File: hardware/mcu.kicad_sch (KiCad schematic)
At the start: 11 parts, among them J12 PICO UTIL, U1 Pico 2

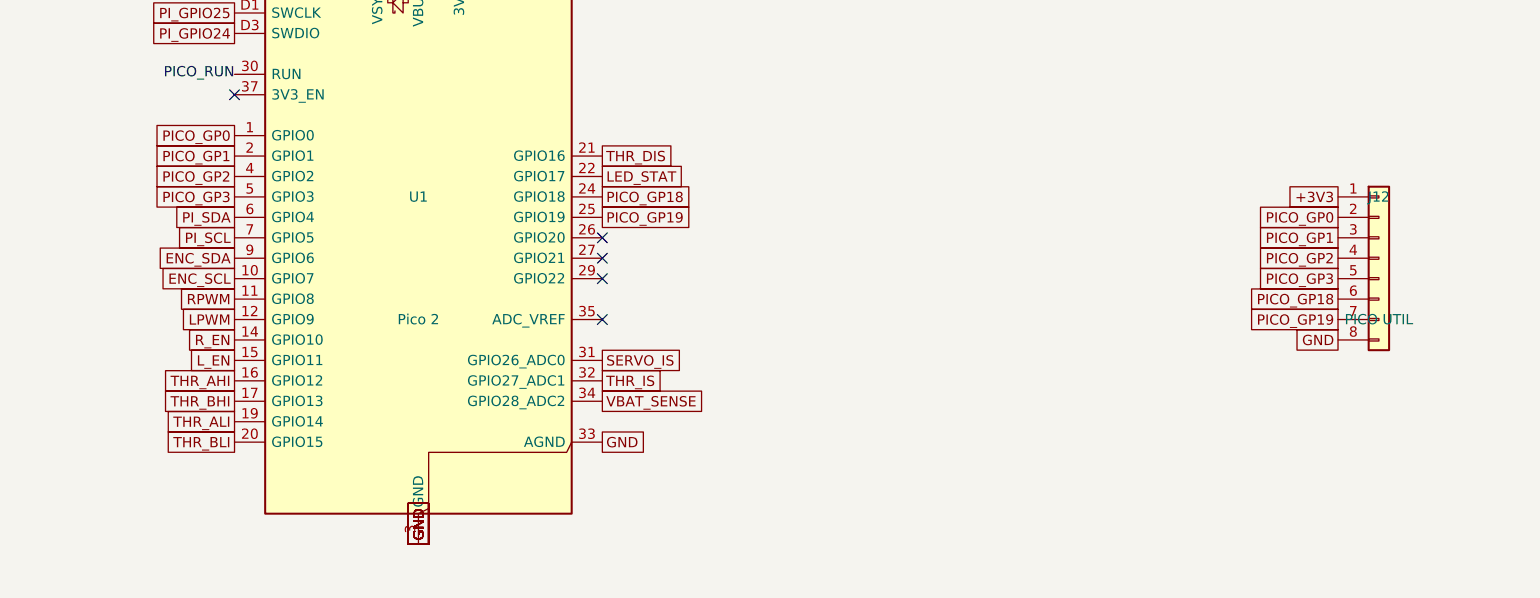
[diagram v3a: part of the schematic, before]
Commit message: cost pass 10 (schematic): remove on-board H-bridge, add J13 external-driver header (IBT-2 pinout); ERC 0, gate PASS
Co-Authored-By: Claude Fable 5 <noreply@anthropic.com>
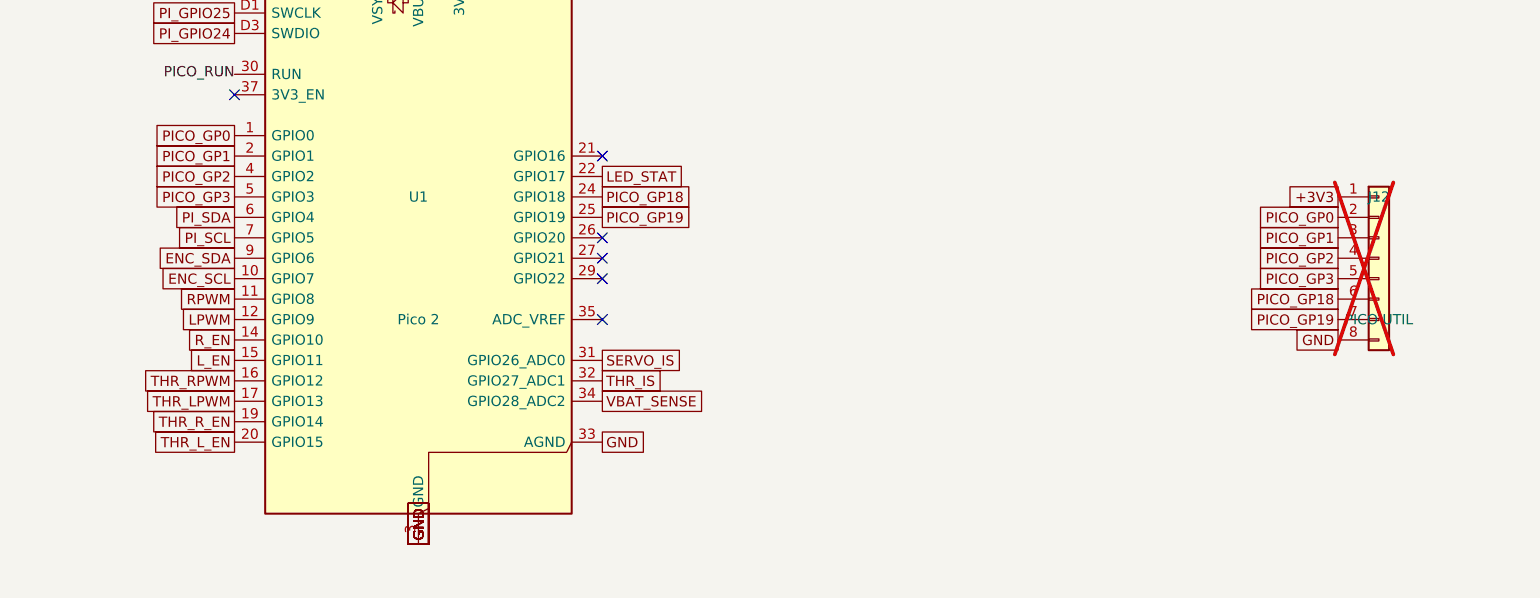
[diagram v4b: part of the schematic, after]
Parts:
- J12: now not fitted
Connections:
- net THR_AHI renamed THR_RPWM
- net THR_ALI renamed THR_R_EN
- net THR_BHI renamed THR_LPWM
- net THR_BLI renamed THR_L_EN
- net THR_DIS: no longer names the net of U1.21 (GPIO16)
- no-connect marks 6 -> 7
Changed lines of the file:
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@@
   )
   (symbol (lib_id "Connector_Generic:Conn_01x08") (at 199.39 110.49 0) (unit 1)
-    (exclude_from_sim no) (in_bom yes) (on_board yes) (dnp no)
+    (exclude_from_sim no) (in_bom yes) (on_board yes) (dnp yes)
     (property "Reference" "J12" (at 199.39 102.87 0)
       (effects (font (size 1.27 1.27))))
@@
       (effects (font (size 1.27 1.27)) (hide yes)))
   )
-  (global_label "THR_AHI" (shape passive) (at 57.15 125.73 180.0) (fields_autoplaced yes)
+  (global_label "THR_RPWM" (shape passive) (at 57.15 125.73 180.0) (fields_autoplaced yes)
     (effects (font (size 1.27 1.27)) (justify right))
     (property "Intersheetrefs" "${INTERSHEET_REFS}" (at 57.15 125.73 0)
       (effects (font (size 1.27 1.27)) (hide yes)))
   )
-  (global_label "THR_BHI" (shape passive) (at 57.15 128.27 180.0) (fields_autoplaced yes)
+  (global_label "THR_LPWM" (shape passive) (at 57.15 128.27 180.0) (fields_autoplaced yes)
     (effects (font (size 1.27 1.27)) (justify right))
     (property "Intersheetrefs" "${INTERSHEET_REFS}" (at 57.15 128.27 0)
@@
       (effects (font (size 1.27 1.27)) (hide yes)))
   )
-  (global_label "THR_ALI" (shape passive) (at 57.15 130.81 180.0) (fields_autoplaced yes)
+  (global_label "THR_R_EN" (shape passive) (at 57.15 130.81 180.0) (fields_autoplaced yes)
     (effects (font (size 1.27 1.27)) (justify right))
     (property "Intersheetrefs" "${INTERSHEET_REFS}" (at 57.15 130.81 0)
       (effects (font (size 1.27 1.27)) (hide yes)))
   )
-  (global_label "THR_BLI" (shape passive) (at 57.15 133.35 180.0) (fields_autoplaced yes)
+  (global_label "THR_L_EN" (shape passive) (at 57.15 133.35 180.0) (fields_autoplaced yes)
     (effects (font (size 1.27 1.27)) (justify right))
     (property "Intersheetrefs" "${INTERSHEET_REFS}" (at 57.15 133.35 0)
       (effects (font (size 1.27 1.27)) (hide yes)))
   )
-  (global_label "THR_DIS" (shape passive) (at 102.87 97.79 0.0) (fields_autoplaced yes)
-    (effects (font (size 1.27 1.27)) (justify left))
-    (property "Intersheetrefs" "${INTERSHEET_REFS}" (at 102.87 97.79 0)
-      (effects (font (size 1.27 1.27)) (hide yes)))
-  )
   (global_label "LED_STAT" (shape passive) (at 102.87 100.33 0.0) (fields_autoplaced yes)
     (effects (font (size 1.27 1.27)) (justify left))
@@
       (effects (font (size 1.27 1.27)) (hide yes)))
   )
+  (no_connect (at 102.87 97.79))
   (no_connect (at 102.87 107.95))
   (no_connect (at 102.87 110.49))

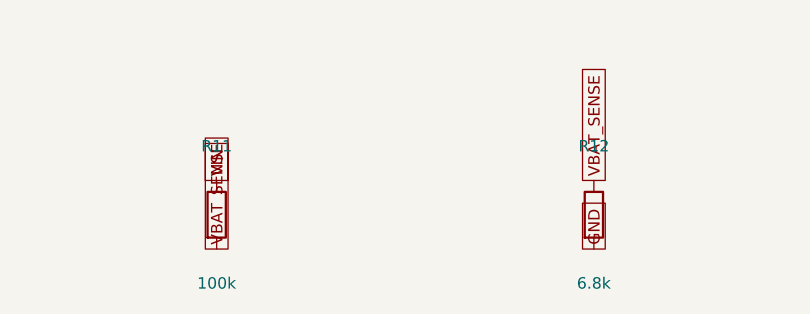
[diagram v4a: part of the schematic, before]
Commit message: feat: v3.1 12V-only — generic 5V buck module on J14, U5/U6/J17 removed, SMCJ18A TVS, servo direct on VIN; DRC clean
Co-Authored-By: Claude Fable 5 <noreply@anthropic.com>
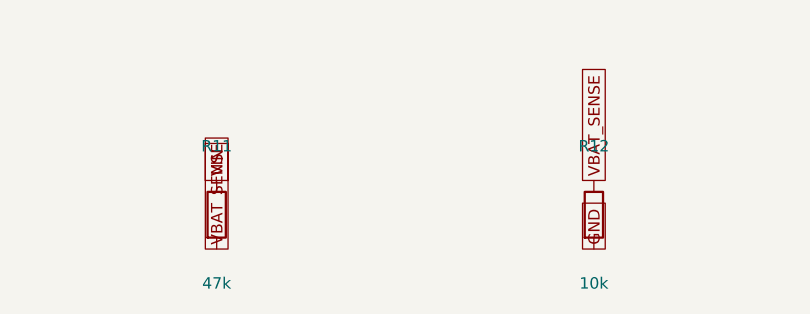
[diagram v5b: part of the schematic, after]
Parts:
- R11: value 100k -> 47k
- R12: value 6.8k -> 10k
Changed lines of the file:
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@@
     (property "Reference" "R11" (at 166.37 162.56 0)
       (effects (font (size 1.27 1.27))))
-    (property "Value" "100k" (at 166.37 177.8 0)
+    (property "Value" "47k" (at 166.37 177.8 0)
       (effects (font (size 1.27 1.27))))
     (property "Footprint" "Resistor_THT:R_Axial_DIN0207_L6.3mm_D2.5mm_P10.16mm_Horizontal" (at 166.37 170.18 0)
@@
     (property "Reference" "R12" (at 208.28 162.56 0)
       (effects (font (size 1.27 1.27))))
-    (property "Value" "6.8k" (at 208.28 177.8 0)
+    (property "Value" "10k" (at 208.28 177.8 0)
       (effects (font (size 1.27 1.27))))
     (property "Footprint" "Resistor_THT:R_Axial_DIN0207_L6.3mm_D2.5mm_P10.16mm_Horizontal" (at 208.28 170.18 0)
